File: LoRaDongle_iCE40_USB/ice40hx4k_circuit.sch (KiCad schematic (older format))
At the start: 3 parts

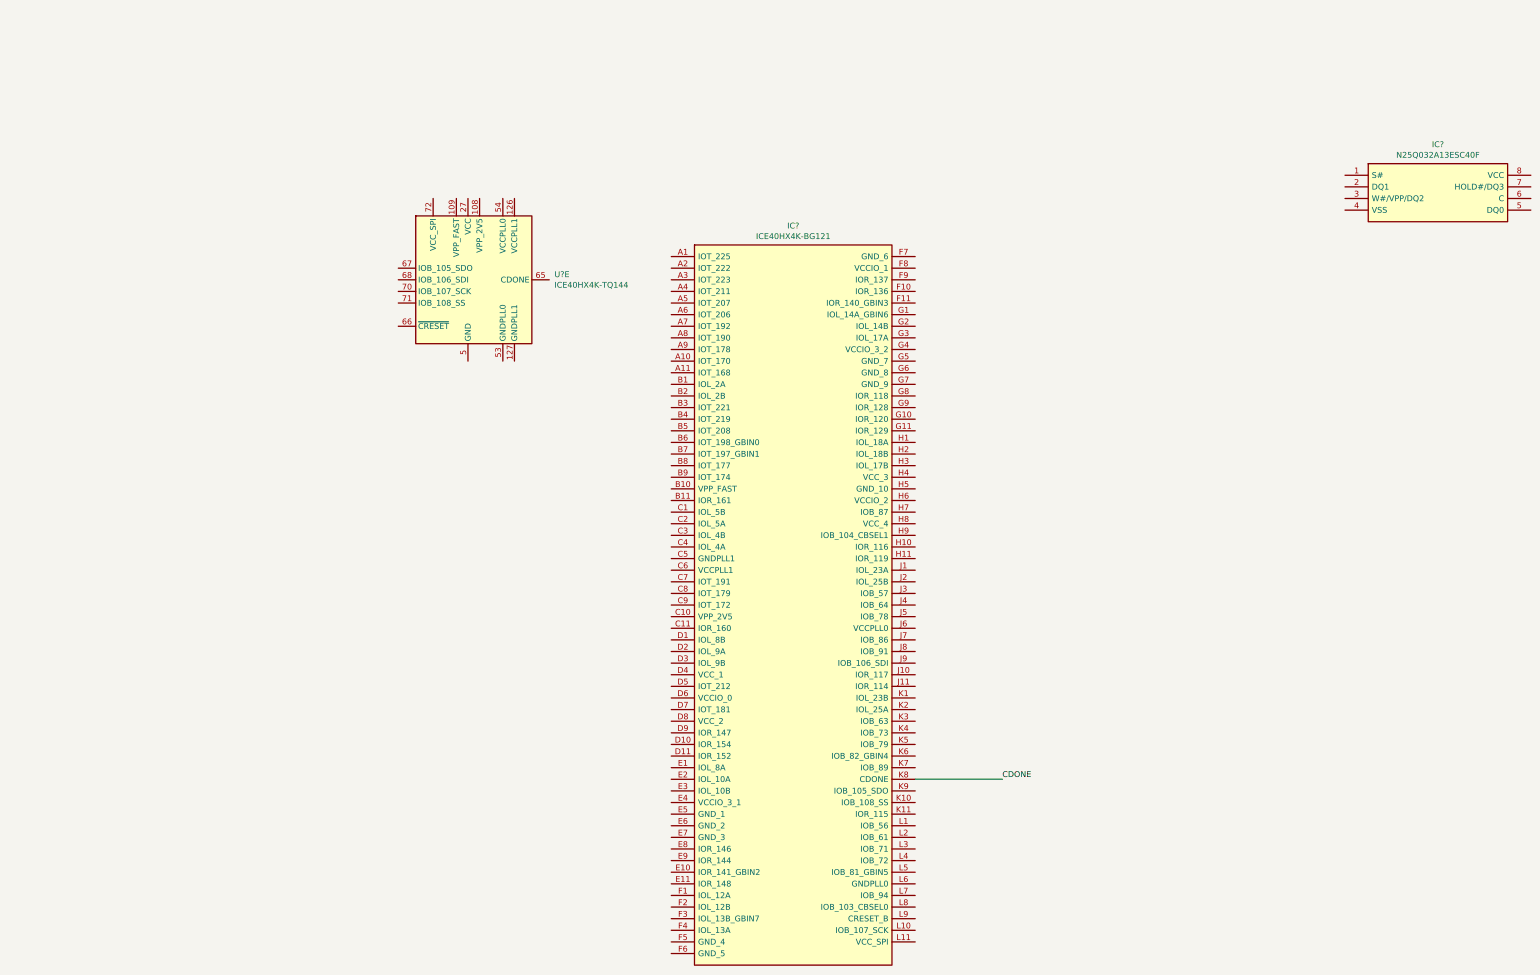
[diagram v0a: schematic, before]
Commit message: initial changes to iCE40UP5k
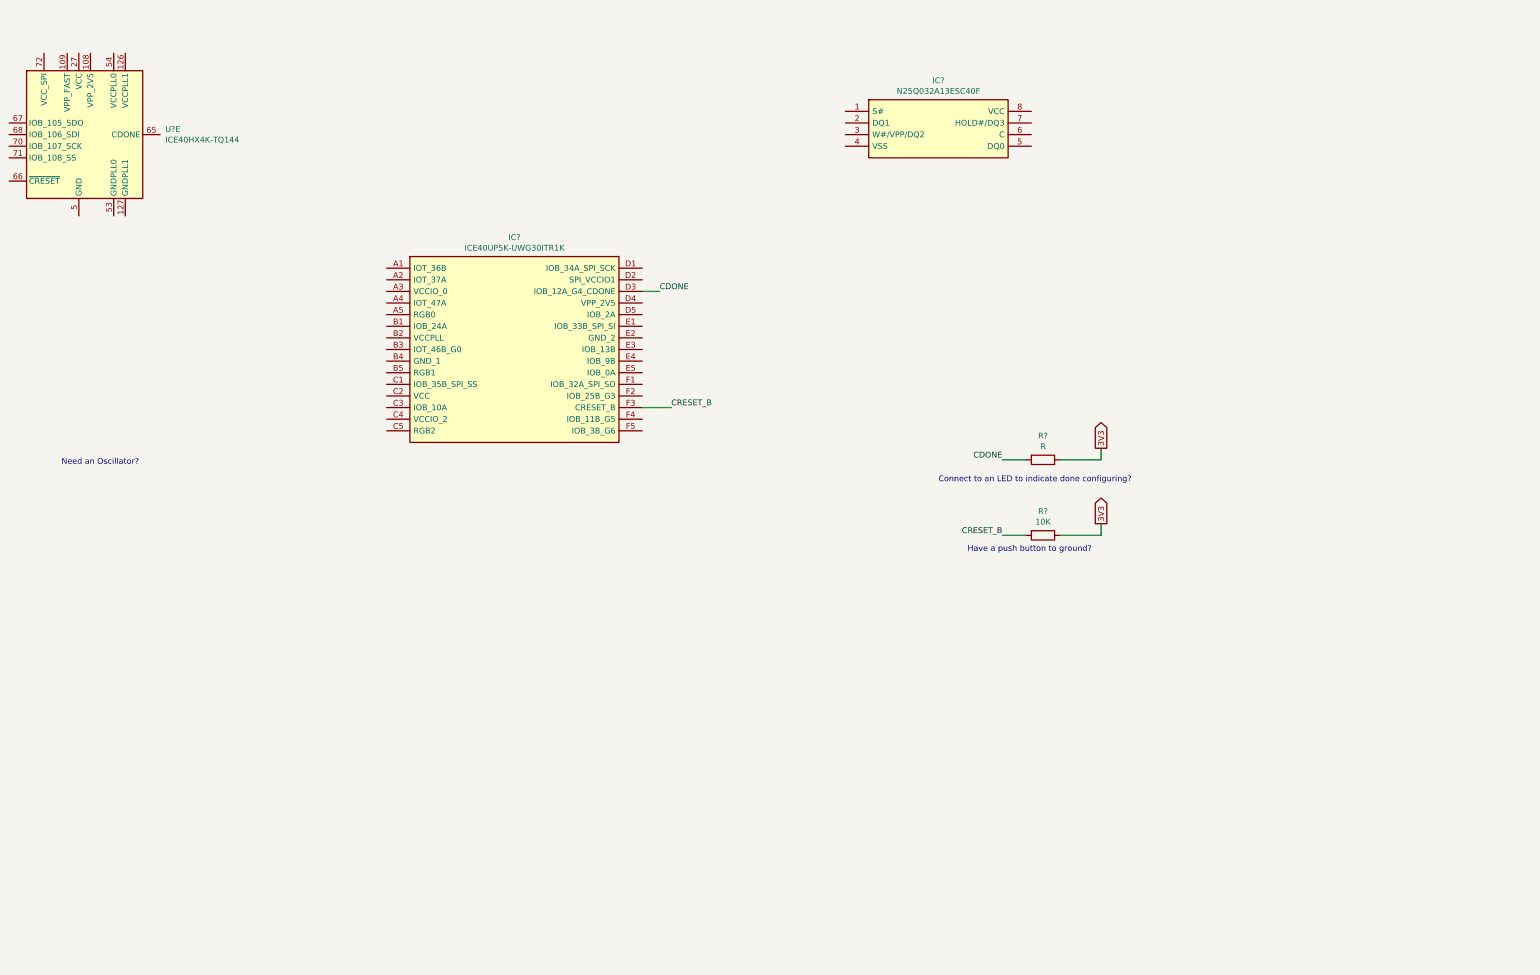
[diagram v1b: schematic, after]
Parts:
- removed IC?: ICE40HX4K-BG121, BGA121C80P11X11_900X900X110, symbol ICE40HX4K-BG121:ICE40HX4K-BG121
- added IC?: ICE40UP5K-UWG30ITR1K, BGA30C40P5X6_211X254X60, symbol ICE40UP5K-UWG30ITR1K:ICE40UP5K-UWG30ITR1K
- added R?: 10K, symbol Device:R
- added R?: R, symbol Device:R
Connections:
- net CDONE: now also IC?.D3 (IOB_12A_G4_CDONE), R?.2
- new net 3V3: R?.1, R?.1
- new net CRESET_B: IC?.F3 (CRESET_B), R?.2
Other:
- note added: "Connect to an LED to indicate done configuring?"
- note added: "Have a push button to ground?"
- note added: "Need an Oscillator?"
- moved on the sheet: IC?, U?E
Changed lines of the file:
@@
 EELAYER 30 0
 EELAYER END
-$Descr A3 16535 11693
+$Descr A4 11693 8268
 encoding utf-8
-Sheet 6 5
+Sheet 4 5
 Title ""
 Date ""
@@
 $EndDescr
 $Comp
-L ICE40HX4K-BG121:ICE40HX4K-BG121 IC?
-U 1 1 61986C08
-P 6700 2750
-F 0 "IC?" H 7750 3015 50  0000 C CNN
-F 1 "ICE40HX4K-BG121" H 7750 2924 50  0000 C CNN
-F 2 "BGA121C80P11X11_900X900X110" H 8650 2850 50  0001 L CNN
-F 3 "http://www.latticesemi.com/iCE40" H 8650 2750 50  0001 L CNN
-F 4 "IC FPGA 93 I/O 121CABGA" H 8650 2650 50  0001 L CNN "Description"
-F 5 "1.1" H 8650 2550 50  0001 L CNN "Height"
-F 6 "Lattice Semiconductor" H 8650 2450 50  0001 L CNN "Manufacturer_Name"
-F 7 "ICE40HX4K-BG121" H 8650 2350 50  0001 L CNN "Manufacturer_Part_Number"
-F 8 "842-ICE40HX4K-BG121" H 8650 2250 50  0001 L CNN "Mouser Part Number"
-F 9 "https://www.mouser.co.uk/ProductDetail/Lattice/ICE40HX4K-BG121?qs=r5DSvlrkXmJ1BLZOg5%2FxBQ%3D%3D" H 8650 2150 50  0001 L CNN "Mouser Price/Stock"
-F 10 "ICE40HX4K-BG121" H 8650 2050 50  0001 L CNN "Arrow Part Number"
-F 11 "https://www.arrow.com/en/products/ice40hx4k-bg121/lattice-semiconductor?region=nac" H 8650 1950 50  0001 L CNN "Arrow Price/Stock"
-	1    6700 2750
+L FPGA_Lattice:ICE40HX4K-TQ144 U?
+U 5 1 619BAE82
+P 1600 1700
+F 0 "U?" H 2344 1746 50  0000 L CNN
+F 1 "ICE40HX4K-TQ144" H 2344 1655 50  0000 L CNN
+F 2 "Package_QFP:TQFP-144_20x20mm_P0.5mm" H 2600 -200 50  0001 R CNN
+F 3 "http://www.latticesemi.com/Products/FPGAandCPLD/iCE40" H 600 4200 50  0001 C CNN
+	5    1600 1700
 	1    0    0    -1
 $EndComp
 $Comp
-L FPGA_Lattice:ICE40HX4K-TQ144 U?
-U 5 1 619BAE82
-P 4950 2950
-F 0 "U?" H 5694 2996 50  0000 L CNN
-F 1 "ICE40HX4K-TQ144" H 5694 2905 50  0000 L CNN
-F 2 "Package_QFP:TQFP-144_20x20mm_P0.5mm" H 5950 1050 50  0001 R CNN
-F 3 "http://www.latticesemi.com/Products/FPGAandCPLD/iCE40" H 3950 5450 50  0001 C CNN
-	5    4950 2950
+L N25Q032A13ESC40F:N25Q032A13ESC40F IC?
+U 1 1 619D2169
+P 9050 1650
+F 0 "IC?" H 9000 2065 50  0000 C CNN
+F 1 "N25Q032A13ESC40F" H 9000 1974 50  0000 C CNN
+F 2 "SOIC127P600X175-8N" H 10600 1750 50  0001 L CNN
+F 3 "https://media-www.micron.com/-/media/client/global/documents/products/data-sheet/nor-flash/serial-nor/n25q/n25q_32mb_3v_65nm.pdf?rev=27fc6016fc5249adb4bb8f221e72b395" H 10600 1650 50  0001 L CNN
+F 4 "FLASH - NOR Memory IC 32Mb (8M x 4) SPI 108MHz  8-SO" H 10600 1550 50  0001 L CNN "Description"
+F 5 "1.75" H 10600 1450 50  0001 L CNN "Height"
+F 6 "Alliance Memory" H 10600 1350 50  0001 L CNN "Manufacturer_Name"
+F 7 "N25Q032A13ESC40F" H 10600 1250 50  0001 L CNN "Manufacturer_Part_Number"
+F 8 "913-N25Q032A13ESC40F" H 10600 1150 50  0001 L CNN "Mouser Part Number"
+F 9 "https://www.mouser.co.uk/ProductDetail/Alliance-Memory/N25Q032A13ESC40F?qs=W%2FMpXkg%252BdQ70%2FmLJsMq3Ww%3D%3D" H 10600 1050 50  0001 L CNN "Mouser Price/Stock"
+F 10 "" H 10600 950 50  0001 L CNN "Arrow Part Number"
+F 11 "" H 10600 850 50  0001 L CNN "Arrow Price/Stock"
+	1    9050 1650
+	1    0    0    -1
+$EndComp
+Text Label 9550 5150 2    50   ~ 0
+CRESET_B
+Text Notes 9250 5300 0    50   ~ 0
+Have a push button to ground?
+Wire Wire Line
+	9750 5150 9550 5150
+Wire Wire Line
+	10400 5150 10400 5050
+Wire Wire Line
+	10050 5150 10400 5150
+$Comp
+L Device:R R?
+U 1 1 619E1A4D
+P 9900 5150
+F 0 "R?" V 9693 5150 50  0000 C CNN
+F 1 "10K" V 9784 5150 50  0000 C CNN
+F 2 "" V 9830 5150 50  0001 C CNN
+F 3 "~" H 9900 5150 50  0001 C CNN
+	1    9900 5150
+	0    1    1    0
+$EndComp
+Text Notes 9000 4700 0    50   ~ 0
+Connect to an LED to indicate done configuring?
+Text Label 9550 4500 2    50   ~ 0
+CDONE
+$Comp
+L Device:R R?
+U 1 1 619F47BF
+P 9900 4500
+F 0 "R?" V 9693 4500 50  0000 C CNN
+F 1 "R" V 9784 4500 50  0000 C CNN
+F 2 "" V 9830 4500 50  0001 C CNN
+F 3 "~" H 9900 4500 50  0001 C CNN
+	1    9900 4500
+	0    1    1    0
+$EndComp
+Wire Wire Line
+	10050 4500 10400 4500
+Wire Wire Line
+	10400 4500 10400 4400
+Text GLabel 10400 4400 1    50   Output ~ 0
+3V3
+Wire Wire Line
+	9750 4500 9550 4500
+Text GLabel 10400 5050 1    50   Output ~ 0
+3V3
+$Comp
+L ICE40UP5K-UWG30ITR1K:ICE40UP5K-UWG30ITR1K IC?
+U 1 1 61AF95E0
+P 4250 2850
+F 0 "IC?" H 5350 3115 50  0000 C CNN
+F 1 "ICE40UP5K-UWG30ITR1K" H 5350 3024 50  0000 C CNN
+F 2 "BGA30C40P5X6_211X254X60" H 6300 2950 50  0001 L CNN
+F 3 "http://www.latticesemi.com/-/media/LatticeSemi/Documents/DataSheets/iCE/FPGA-DS-02008-1-6-iCE40-UltraPlus-Family-Data-Sheet.ashx?document_id=51968" H 6300 2850 50  0001 L CNN
+F 4 "FPGA - Field Programmable Gate Array iCE40-UltraPlus, 5280 LUTs, 1.2V" H 6300 2750 50  0001 L CNN "Description"
+F 5 "0.6" H 6300 2650 50  0001 L CNN "Height"
+F 6 "Lattice Semiconductor" H 6300 2550 50  0001 L CNN "Manufacturer_Name"
+F 7 "ICE40UP5K-UWG30ITR1K" H 6300 2450 50  0001 L CNN "Manufacturer_Part_Number"
+F 8 "842-40UP5KUWG30ITR1K" H 6300 2350 50  0001 L CNN "Mouser Part Number"
+F 9 "https://www.mouser.co.uk/ProductDetail/Lattice/ICE40UP5K-UWG30ITR1K?qs=Rp3RbKSfAt0rwndd2oX17g%3D%3D" H 6300 2250 50  0001 L CNN "Mouser Price/Stock"
+F 10 "ICE40UP5K-UWG30ITR1K" H 6300 2150 50  0001 L CNN "Arrow Part Number"
+F 11 "https://www.arrow.com/en/products/ice40up5k-uwg30itr1k/lattice-semiconductor?region=nac" H 6300 2050 50  0001 L CNN "Arrow Price/Stock"
+	1    4250 2850
 	1    0    0    -1
 $EndComp
 Wire Wire Line
-	8800 7250 9550 7250
-Text Label 9550 7250 0    50   ~ 0
+	6450 3050 6600 3050
+Wire Wire Line
+	6450 4050 6700 4050
+Text Label 6600 3050 0    50   ~ 0
 CDONE
-$Comp
-L N25Q032A13ESC40F:N25Q032A13ESC40F IC?
-U 1 1 619D2169
-P 13350 2200
-F 0 "IC?" H 13300 2615 50  0000 C CNN
-F 1 "N25Q032A13ESC40F" H 13300 2524 50  0000 C CNN
-F 2 "SOIC127P600X175-8N" H 14900 2300 50  0001 L CNN
-F 3 "https://media-www.micron.com/-/media/client/global/documents/products/data-sheet/nor-flash/serial-nor/n25q/n25q_32mb_3v_65nm.pdf?rev=27fc6016fc5249adb4bb8f221e72b395" H 14900 2200 50  0001 L CNN
-F 4 "FLASH - NOR Memory IC 32Mb (8M x 4) SPI 108MHz  8-SO" H 14900 2100 50  0001 L CNN "Description"
-F 5 "1.75" H 14900 2000 50  0001 L CNN "Height"
-F 6 "Alliance Memory" H 14900 1900 50  0001 L CNN "Manufacturer_Name"
-F 7 "N25Q032A13ESC40F" H 14900 1800 50  0001 L CNN "Manufacturer_Part_Number"
-F 8 "913-N25Q032A13ESC40F" H 14900 1700 50  0001 L CNN "Mouser Part Number"
-F 9 "https://www.mouser.co.uk/ProductDetail/Alliance-Memory/N25Q032A13ESC40F?qs=W%2FMpXkg%252BdQ70%2FmLJsMq3Ww%3D%3D" H 14900 1600 50  0001 L CNN "Mouser Price/Stock"
-F 10 "" H 14900 1500 50  0001 L CNN "Arrow Part Number"
-F 11 "" H 14900 1400 50  0001 L CNN "Arrow Price/Stock"
-	1    13350 2200
-	1    0    0    -1
-$EndComp
+Text Label 6700 4050 0    50   ~ 0
+CRESET_B
+Text Notes 1450 4550 0    50   ~ 0
+Need an Oscillator?
 $EndSCHEMATC

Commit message: changed to sx1261
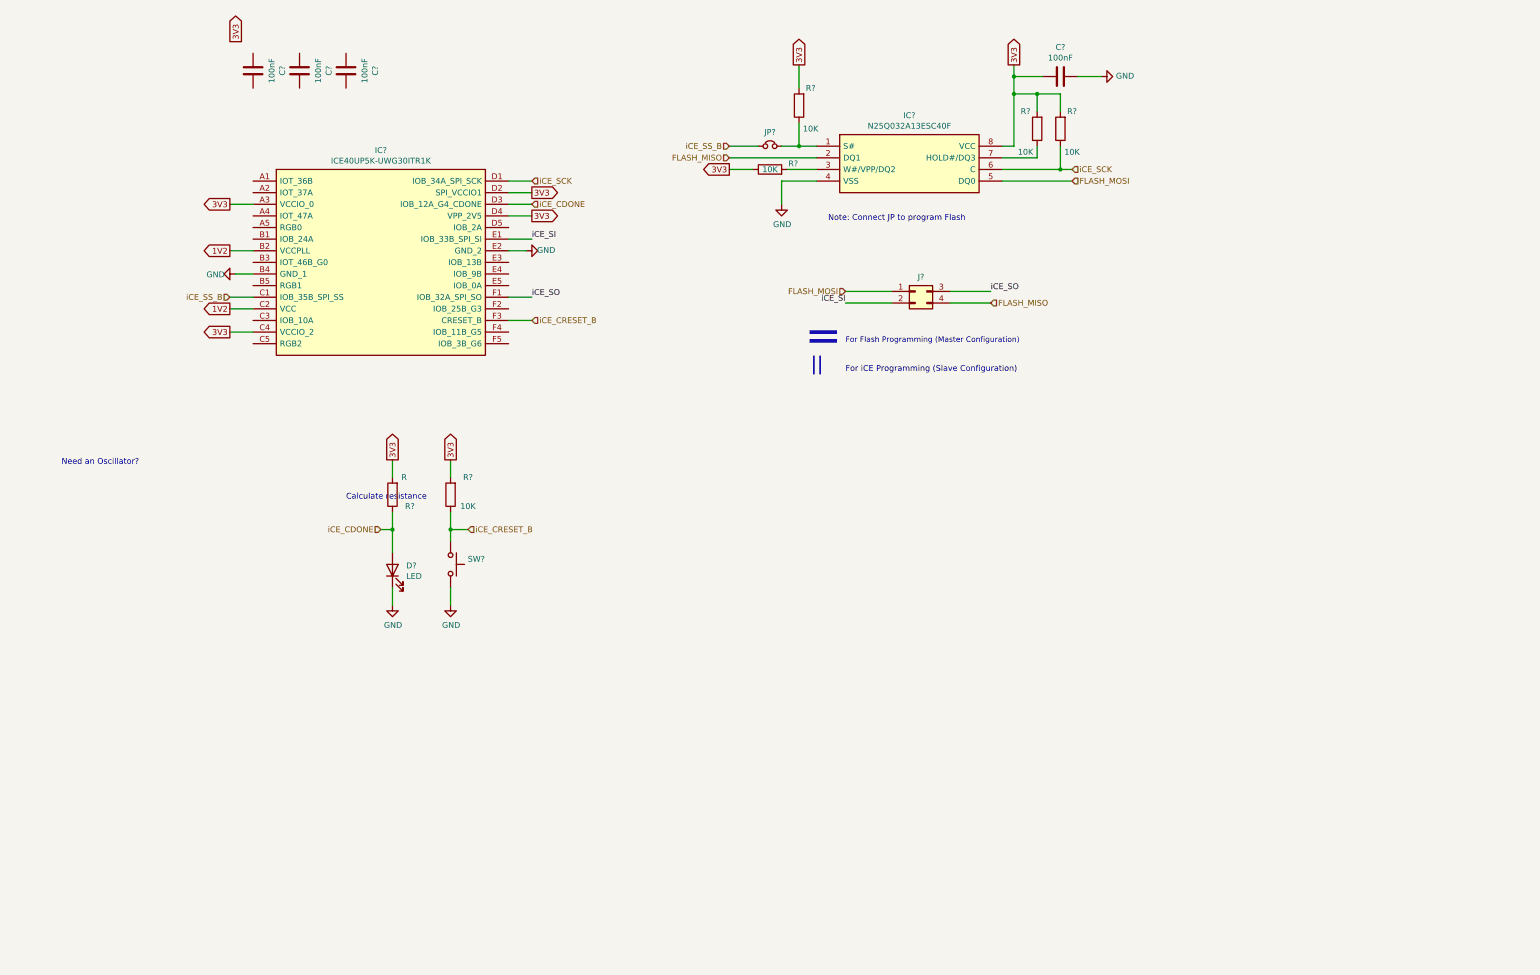
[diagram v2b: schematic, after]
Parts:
- removed U?: ICE40HX4K-TQ144, Package_QFP:TQFP-144_20x20mm_P0.5mm, symbol FPGA_Lattice:ICE40HX4K-TQ144
- added C? (x4): 100nF, symbol Device:C
- added D?: LED, symbol Device:LED
- added J?: Conn_02x02_Top_Bottom, Connector_PinHeader_1.00mm:PinHeader_2x02_P1.00mm_Vertical, symbol Connector_Generic:Conn_02x02_Top_Bottom
- added JP?: Jumper_NC_Small, symbol Device:Jumper_NC_Small
- added R? (x4): 10K, symbol Device:R
- added SW?: SW_Push, symbol Switch:SW_Push
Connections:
- net 3V3: now also IC?.8 (VCC), IC?.A3 (VCCIO_0), IC?.C4 (VCCIO_2), IC?.D2 (SPI_VCCIO1), IC?.D4 (VPP_2V5), R?.2, R?.2, C?.2, R?.1, R?.2, R?.2, R?.2; no longer R?.1, R?.1
- net at IC?.1 (S#): now also JP?.2, R?.1
- net FLASH_MISO: now reaches IC?.2 (DQ1)
- net FLASH_MISO: now also J?.4 (Pin_4)
- net at IC?.3 (W#/VPP/DQ2): now also R?.2
- net GND: now reaches IC?.4 (VSS)
- net GND: now also IC?.B4 (GND_1), IC?.E2 (GND_2), C?.1, D?.1 (K), SW?.2
- net FLASH_MOSI: now reaches IC?.5 (DQ0)
- net FLASH_MOSI: now also J?.1 (Pin_1)
- net iCE_SCK: now reaches IC?.6 (C)
- net iCE_SCK: now also IC?.D1 (IOB_34A_SPI_SCK), R?.1
- net at IC?.7 (HOLD#/DQ3): now also R?.1
- net 1V2: now reaches IC?.B2 (VCCPLL)
- net 1V2: now also IC?.C2 (VCC)
- net iCE_SS_B: now reaches IC?.C1 (IOB_35B_SPI_SS)
- net iCE_SS_B: now also JP?.1
- net iCE_SI: now reaches IC?.E1 (IOB_33B_SPI_SI)
- net iCE_SI: now also J?.2 (Pin_2)
- net iCE_SO: now reaches IC?.F1 (IOB_32A_SPI_SO)
- net iCE_SO: now also J?.3 (Pin_3)
- net CDONE renamed iCE_CDONE
- net iCE_CDONE: now also R?.1, D?.2 (A); no longer R?.2
- net CRESET_B renamed iCE_CRESET_B
- net iCE_CRESET_B: now also R?.1, SW?.1; no longer R?.2
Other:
- note added: "="
- note added: "Calculate resistance"
- note added: "For Flash Programming (Master Configuration)"
- note added: "For iCE Programming (Slave Configuration)"
- note added: "Note: Connect JP to program Flash"
- note added: "||"
- note removed: "Connect to an LED to indicate done configuring?"
- note removed: "Have a push button to ground?"
- moved on the sheet: IC?, R?
